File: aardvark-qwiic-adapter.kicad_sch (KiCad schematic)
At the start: 1 part, among them J1 Conn_02x05_Odd_Even

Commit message: Add LDO
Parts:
- added U1: AP7361C-33E, Package_TO_SOT_SMD:SOT-223-3_TabPin2, symbol Regulator_Linear:AP7361C-33E
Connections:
- net GND: now also U1.2 (GND)
- net at J1.4 (Pin_4): now also J1.6 (Pin_6), U1.1 (VI)
- new net +3.3V: U1.3 (VO)
- no-connect marks 2 -> 0
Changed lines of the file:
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@@
     (rev "1.0")
   )
-  (no_connect (at 148.59 93.98))
-  (no_connect (at 148.59 96.52))
+  (junction (at 151.13 93.98) (diameter 0) (color 0 0 0 0)
+  )
+  (wire (pts (xy 185.42 93.98) (xy 190.5 93.98))
+    (stroke (width 0) (type default))
+  )
   (wire (pts (xy 129.54 99.06) (xy 135.89 99.06))
+    (stroke (width 0) (type default))
+  )
+  (wire (pts (xy 190.5 93.98) (xy 190.5 92.71))
+    (stroke (width 0) (type default))
+  )
+  (wire (pts (xy 151.13 93.98) (xy 151.13 96.52))
     (stroke (width 0) (type default))
   )
@@
     (stroke (width 0) (type default))
   )
+  (wire (pts (xy 148.59 93.98) (xy 151.13 93.98))
+    (stroke (width 0) (type default))
+  )
+  (wire (pts (xy 151.13 93.98) (xy 170.18 93.98))
+    (stroke (width 0) (type default))
+  )
   (wire (pts (xy 148.59 91.44) (xy 156.21 91.44))
     (stroke (width 0) (type default))
@@
     (stroke (width 0) (type default))
   )
+  (wire (pts (xy 148.59 96.52) (xy 151.13 96.52))
+    (stroke (width 0) (type default))
+  )
   (wire (pts (xy 129.54 96.52) (xy 135.89 96.52))
+    (stroke (width 0) (type default))
+  )
+  (wire (pts (xy 177.8 101.6) (xy 177.8 102.87))
     (stroke (width 0) (type default))
   )
@@
     (effects (font (size 1.27 1.27)) (justify right bottom))
   )
+  (symbol (lib_id "power:GND") (at 177.8 102.87 0) (unit 1)
+    (in_bom yes) (on_board yes) (dnp no) (fields_autoplaced)
+    (property "Reference" "#PWR02" (at 177.8 109.22 0)
+      (effects (font (size 1.27 1.27)) hide)
+    )
+    (property "Value" "GND" (at 177.8 107.95 0)
+      (effects (font (size 1.27 1.27)))
+    )
+    (property "Footprint" "" (at 177.8 102.87 0)
+      (effects (font (size 1.27 1.27)) hide)
+    )
+    (property "Datasheet" "" (at 177.8 102.87 0)
+      (effects (font (size 1.27 1.27)) hide)
+    )
+    (pin "1")
+    (instances
+      (project "aardvark-qwiic-adapter"
+        (path "/dd35b9f1-2797-46a7-a3ff-4e2c1be5fc91"
+          (reference "#PWR02") (unit 1)
+        )
+      )
+    )
+  )
+  (symbol (lib_id "power:+3.3V") (at 190.5 92.71 0) (unit 1)
+    (in_bom yes) (on_board yes) (dnp no) (fields_autoplaced)
+    (property "Reference" "#PWR01" (at 190.5 96.52 0)
+      (effects (font (size 1.27 1.27)) hide)
+    )
+    (property "Value" "+3.3V" (at 190.5 88.9 0)
+      (effects (font (size 1.27 1.27)))
+    )
+    (property "Footprint" "" (at 190.5 92.71 0)
+      (effects (font (size 1.27 1.27)) hide)
+    )
+    (property "Datasheet" "" (at 190.5 92.71 0)
+      (effects (font (size 1.27 1.27)) hide)
+    )
+    (pin "1")
+    (instances
+      (project "aardvark-qwiic-adapter"
+        (path "/dd35b9f1-2797-46a7-a3ff-4e2c1be5fc91"
+          (reference "#PWR01") (unit 1)
+        )
+      )
+    )
+  )
+  (symbol (lib_id "Regulator_Linear:AP7361C-33E") (at 177.8 93.98 0) (unit 1)
+    (in_bom yes) (on_board yes) (dnp no) (fields_autoplaced)
+    (property "Reference" "U1" (at 177.8 87.63 0)
+      (effects (font (size 1.27 1.27)))
+    )
+    (property "Value" "AP7361C-33E" (at 177.8 90.17 0)
+      (effects (font (size 1.27 1.27)))
+    )
+    (property "Footprint" "Package_TO_SOT_SMD:SOT-223-3_TabPin2" (at 177.8 88.265 0)
+      (effects (font (size 1.27 1.27) italic) hide)
+    )
+    (property "Datasheet" "https://www.diodes.com/assets/Datasheets/AP7361C.pdf" (at 177.8 95.25 0)
+      (effects (font (size 1.27 1.27)) hide)
+    )
+    (pin "1")
+    (pin "2")
+    (pin "3")
+    (instances
+      (project "aardvark-qwiic-adapter"
+        (path "/dd35b9f1-2797-46a7-a3ff-4e2c1be5fc91"
+          (reference "U1") (unit 1)
+        )
+      )
+    )
+  )
   (symbol (lib_id "Connector_Generic:Conn_02x05_Odd_Even") (at 140.97 96.52 0) (unit 1)

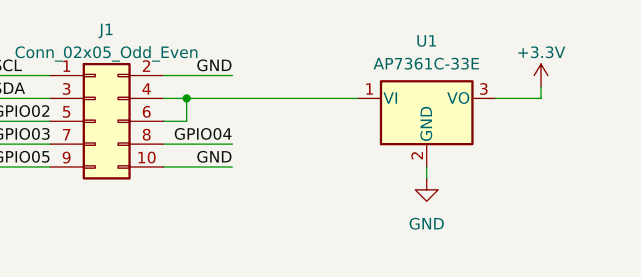
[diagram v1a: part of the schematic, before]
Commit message: Caps on LDO
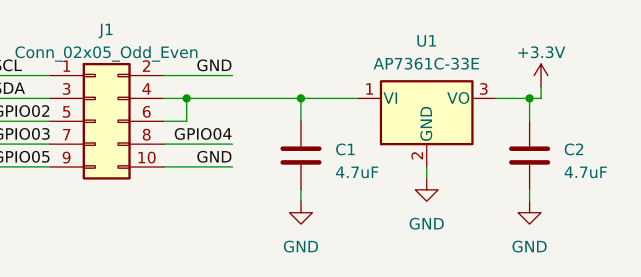
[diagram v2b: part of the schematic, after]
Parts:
- added C1, C2: 4.7uF, Capacitor_SMD:C_0805_2012Metric, symbol Device:C
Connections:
- net +3.3V: now also C2.1
- net GND: now also C1.2, C2.2
- net at J1.4 (Pin_4), J1.6 (Pin_6), U1.1 (VI): now also C1.1
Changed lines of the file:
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@@
   (junction (at 151.13 93.98) (diameter 0) (color 0 0 0 0)
   )
-  (wire (pts (xy 185.42 93.98) (xy 190.5 93.98))
+  (junction (at 189.23 93.98) (diameter 0) (color 0 0 0 0)
+  )
+  (junction (at 163.83 93.98) (diameter 0) (color 0 0 0 0)
+  )
+  (wire (pts (xy 163.83 93.98) (xy 170.18 93.98))
+    (stroke (width 0) (type default))
+  )
+  (wire (pts (xy 163.83 93.98) (xy 163.83 96.52))
+    (stroke (width 0) (type default))
+  )
+  (wire (pts (xy 185.42 93.98) (xy 189.23 93.98))
     (stroke (width 0) (type default))
   )
@@
     (stroke (width 0) (type default))
   )
+  (wire (pts (xy 189.23 93.98) (xy 189.23 96.52))
+    (stroke (width 0) (type default))
+  )
   (wire (pts (xy 129.54 101.6) (xy 135.89 101.6))
     (stroke (width 0) (type default))
@@
     (stroke (width 0) (type default))
   )
-  (wire (pts (xy 151.13 93.98) (xy 170.18 93.98))
+  (wire (pts (xy 151.13 93.98) (xy 163.83 93.98))
     (stroke (width 0) (type default))
   )
@@
     (stroke (width 0) (type default))
   )
+  (wire (pts (xy 163.83 104.14) (xy 163.83 105.41))
+    (stroke (width 0) (type default))
+  )
   (wire (pts (xy 148.59 96.52) (xy 151.13 96.52))
     (stroke (width 0) (type default))
@@
   )
   (wire (pts (xy 177.8 101.6) (xy 177.8 102.87))
+    (stroke (width 0) (type default))
+  )
+  (wire (pts (xy 189.23 93.98) (xy 190.5 93.98))
+    (stroke (width 0) (type default))
+  )
+  (wire (pts (xy 189.23 104.14) (xy 189.23 105.41))
     (stroke (width 0) (type default))
   )
@@
     (effects (font (size 1.27 1.27)) (justify right bottom))
   )
+  (symbol (lib_id "Device:C") (at 163.83 100.33 0) (unit 1)
+    (in_bom yes) (on_board yes) (dnp no) (fields_autoplaced)
+    (property "Reference" "C1" (at 167.64 99.695 0)
+      (effects (font (size 1.27 1.27)) (justify left))
+    )
+    (property "Value" "4.7uF" (at 167.64 102.235 0)
+      (effects (font (size 1.27 1.27)) (justify left))
+    )
+    (property "Footprint" "Capacitor_SMD:C_0805_2012Metric" (at 164.7952 104.14 0)
+      (effects (font (size 1.27 1.27)) hide)
+    )
+    (property "Datasheet" "~" (at 163.83 100.33 0)
+      (effects (font (size 1.27 1.27)) hide)
+    )
+    (pin "1")
+    (pin "2")
+    (instances
+      (project "aardvark-qwiic-adapter"
+        (path "/dd35b9f1-2797-46a7-a3ff-4e2c1be5fc91"
+          (reference "C1") (unit 1)
+        )
+      )
+    )
+  )
+  (symbol (lib_id "power:GND") (at 163.83 105.41 0) (unit 1)
+    (in_bom yes) (on_board yes) (dnp no) (fields_autoplaced)
+    (property "Reference" "#PWR03" (at 163.83 111.76 0)
+      (effects (font (size 1.27 1.27)) hide)
+    )
+    (property "Value" "GND" (at 163.83 110.49 0)
+      (effects (font (size 1.27 1.27)))
+    )
+    (property "Footprint" "" (at 163.83 105.41 0)
+      (effects (font (size 1.27 1.27)) hide)
+    )
+    (property "Datasheet" "" (at 163.83 105.41 0)
+      (effects (font (size 1.27 1.27)) hide)
+    )
+    (pin "1")
+    (instances
+      (project "aardvark-qwiic-adapter"
+        (path "/dd35b9f1-2797-46a7-a3ff-4e2c1be5fc91"
+          (reference "#PWR03") (unit 1)
+        )
+      )
+    )
+  )
+  (symbol (lib_id "power:GND") (at 189.23 105.41 0) (unit 1)
+    (in_bom yes) (on_board yes) (dnp no) (fields_autoplaced)
+    (property "Reference" "#PWR04" (at 189.23 111.76 0)
+      (effects (font (size 1.27 1.27)) hide)
+    )
+    (property "Value" "GND" (at 189.23 110.49 0)
+      (effects (font (size 1.27 1.27)))
+    )
+    (property "Footprint" "" (at 189.23 105.41 0)
+      (effects (font (size 1.27 1.27)) hide)
+    )
+    (property "Datasheet" "" (at 189.23 105.41 0)
+      (effects (font (size 1.27 1.27)) hide)
+    )
+    (pin "1")
+    (instances
+      (project "aardvark-qwiic-adapter"
+        (path "/dd35b9f1-2797-46a7-a3ff-4e2c1be5fc91"
+          (reference "#PWR04") (unit 1)
+        )
+      )
+    )
+  )
   (symbol (lib_id "power:GND") (at 177.8 102.87 0) (unit 1)
     (in_bom yes) (on_board yes) (dnp no) (fields_autoplaced)
@@
         )
       )
+    )
+  )
+  (symbol (lib_id "Device:C") (at 189.23 100.33 0) (unit 1)
+    (in_bom yes) (on_board yes) (dnp no) (fields_autoplaced)
+    (property "Reference" "C2" (at 193.04 99.695 0)
+      (effects (font (size 1.27 1.27)) (justify left))
+    )
+    (property "Value" "4.7uF" (at 193.04 102.235 0)
+      (effects (font (size 1.27 1.27)) (justify left))
+    )
+    (property "Footprint" "Capacitor_SMD:C_0805_2012Metric" (at 190.1952 104.14 0)
+      (effects (font (size 1.27 1.27)) hide)
+    )
+    (property "Datasheet" "~" (at 189.23 100.33 0)
+      (effects (font (size 1.27 1.27)) hide)
+    )
+    (pin "1")
+    (pin "2")
+    (instances
+      (project "aardvark-qwiic-adapter"
+        (path "/dd35b9f1-2797-46a7-a3ff-4e2c1be5fc91"
+          (reference "C2") (unit 1)
+        )
+      )

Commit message: QWIIC connector
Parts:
- added J2: Conn_01x04, Connector_JST:JST_SH_BM04B-SRSS-TB_1x04-1MP_P1.00mm_Vertical, symbol Connector_Generic:Conn_01x04
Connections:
- net +3.3V: now also J2.3 (Pin_3)
- net GND: now also J2.4 (Pin_4)
- net SCL: now also J2.1 (Pin_1)
- net SDA: now also J2.2 (Pin_2)
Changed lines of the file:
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@@
+    (stroke (width 0) (type default))
+  )
+  (wire (pts (xy 83.82 96.52) (xy 91.44 96.52))
     (stroke (width 0) (type default))
   )
@@
     (stroke (width 0) (type default))
   )
+  (wire (pts (xy 83.82 99.06) (xy 91.44 99.06))
+    (stroke (width 0) (type default))
+  )
   (wire (pts (xy 189.23 93.98) (xy 189.23 96.52))
     (stroke (width 0) (type default))
@@
     (stroke (width 0) (type default))
   )
+  (wire (pts (xy 83.82 93.98) (xy 91.44 93.98))
+    (stroke (width 0) (type default))
+  )
   (wire (pts (xy 148.59 91.44) (xy 156.21 91.44))
     (stroke (width 0) (type default))
@@
   )
   (wire (pts (xy 148.59 96.52) (xy 151.13 96.52))
+    (stroke (width 0) (type default))
+  )
+  (wire (pts (xy 83.82 91.44) (xy 91.44 91.44))
     (stroke (width 0) (type default))
   )
@@
     (effects (font (size 1.27 1.27)) (justify right bottom))
   )
+  (label "GND" (at 83.82 99.06 0) (fields_autoplaced)
+    (effects (font (size 1.27 1.27)) (justify left bottom))
+  )
+  (label "SDA" (at 83.82 93.98 0) (fields_autoplaced)
+    (effects (font (size 1.27 1.27)) (justify left bottom))
+  )
+  (label "SCL" (at 83.82 91.44 0) (fields_autoplaced)
+    (effects (font (size 1.27 1.27)) (justify left bottom))
+  )
+  (label "+3.3V" (at 83.82 96.52 0) (fields_autoplaced)
+    (effects (font (size 1.27 1.27)) (justify left bottom))
+  )
   (symbol (lib_id "Device:C") (at 163.83 100.33 0) (unit 1)
     (in_bom yes) (on_board yes) (dnp no) (fields_autoplaced)
@@
         )
       )
+    )
+  )
+  (symbol (lib_id "Connector_Generic:Conn_01x04") (at 96.52 93.98 0) (unit 1)
+    (in_bom yes) (on_board yes) (dnp no) (fields_autoplaced)
+    (property "Reference" "J2" (at 99.06 94.615 0)
+      (effects (font (size 1.27 1.27)) (justify left))
+    )
+    (property "Value" "Conn_01x04" (at 99.06 97.155 0)
+      (effects (font (size 1.27 1.27)) (justify left))
+    )
+    (property "Footprint" "Connector_JST:JST_SH_BM04B-SRSS-TB_1x04-1MP_P1.00mm_Vertical" (at 96.52 93.98 0)
+      (effects (font (size 1.27 1.27)) hide)
+    )
+    (property "Datasheet" "~" (at 96.52 93.98 0)
+      (effects (font (size 1.27 1.27)) hide)
+    )
+    (pin "1")
+    (pin "2")
+    (pin "3")
+    (pin "4")
+    (instances
+      (project "aardvark-qwiic-adapter"
+        (path "/dd35b9f1-2797-46a7-a3ff-4e2c1be5fc91"
+          (reference "J2") (unit 1)
+        )
+      )

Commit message: Title block
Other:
- title: Aardvark I2C Breakout -> Aardvark QWIIC Adapter
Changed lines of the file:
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@@
   (paper "USLetter")
   (title_block
-    (title "Aardvark I2C Breakout")
-    (date "2023-02-18")
+    (title "Aardvark QWIIC Adapter")
+    (date "2023-02-19")
     (rev "1.0")
   )

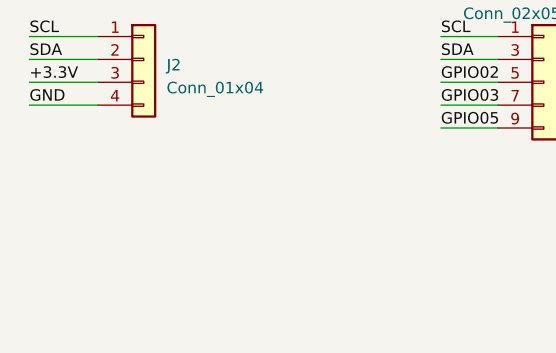
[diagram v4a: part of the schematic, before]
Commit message: GPIO breakout
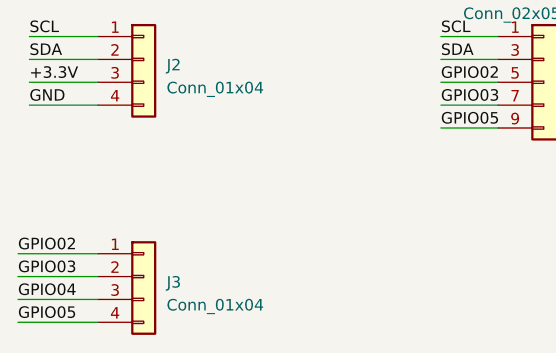
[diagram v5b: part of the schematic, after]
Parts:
- added J3: Conn_01x04, Connector_PinHeader_2.54mm:PinHeader_1x04_P2.54mm_Vertical, symbol Connector_Generic:Conn_01x04
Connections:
- net GPIO02: now also J3.1 (Pin_1)
- net GPIO03: now also J3.2 (Pin_2)
- net GPIO04: now also J3.3 (Pin_3)
- net GPIO05: now also J3.4 (Pin_4)
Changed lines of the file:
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@@
+    (stroke (width 0) (type default))
+  )
+  (wire (pts (xy 82.55 115.57) (xy 91.44 115.57))
     (stroke (width 0) (type default))
   )
@@
     (stroke (width 0) (type default))
   )
+  (wire (pts (xy 82.55 120.65) (xy 91.44 120.65))
+    (stroke (width 0) (type default))
+  )
   (wire (pts (xy 148.59 93.98) (xy 151.13 93.98))
     (stroke (width 0) (type default))
@@
     (stroke (width 0) (type default))
   )
+  (wire (pts (xy 82.55 118.11) (xy 91.44 118.11))
+    (stroke (width 0) (type default))
+  )
   (wire (pts (xy 148.59 99.06) (xy 156.21 99.06))
     (stroke (width 0) (type default))
@@
     (stroke (width 0) (type default))
   )
+  (wire (pts (xy 82.55 123.19) (xy 91.44 123.19))
+    (stroke (width 0) (type default))
+  )
   (wire (pts (xy 189.23 104.14) (xy 189.23 105.41))
     (stroke (width 0) (type default))
@@
   )
   (label "SCL" (at 129.54 91.44 0) (fields_autoplaced)
+    (effects (font (size 1.27 1.27)) (justify left bottom))
+  )
+  (label "GPIO04" (at 82.55 120.65 0) (fields_autoplaced)
     (effects (font (size 1.27 1.27)) (justify left bottom))
   )
@@
     (effects (font (size 1.27 1.27)) (justify right bottom))
   )
+  (label "GPIO05" (at 82.55 123.19 0) (fields_autoplaced)
+    (effects (font (size 1.27 1.27)) (justify left bottom))
+  )
   (label "GND" (at 156.21 101.6 180) (fields_autoplaced)
     (effects (font (size 1.27 1.27)) (justify right bottom))
@@
     (effects (font (size 1.27 1.27)) (justify left bottom))
   )
+  (label "GPIO03" (at 82.55 118.11 0) (fields_autoplaced)
+    (effects (font (size 1.27 1.27)) (justify left bottom))
+  )
+  (label "GPIO02" (at 82.55 115.57 0) (fields_autoplaced)
+    (effects (font (size 1.27 1.27)) (justify left bottom))
+  )
   (label "SDA" (at 129.54 93.98 0) (fields_autoplaced)
     (effects (font (size 1.27 1.27)) (justify left bottom))
@@
         )
       )
+    )
+  )
+  (symbol (lib_id "Connector_Generic:Conn_01x04") (at 96.52 118.11 0) (unit 1)
+    (in_bom yes) (on_board yes) (dnp no) (fields_autoplaced)
+    (property "Reference" "J3" (at 99.06 118.745 0)
+      (effects (font (size 1.27 1.27)) (justify left))
+    )
+    (property "Value" "Conn_01x04" (at 99.06 121.285 0)
+      (effects (font (size 1.27 1.27)) (justify left))
+    )
+    (property "Footprint" "Connector_PinHeader_2.54mm:PinHeader_1x04_P2.54mm_Vertical" (at 96.52 118.11 0)
+      (effects (font (size 1.27 1.27)) hide)
+    )
+    (property "Datasheet" "~" (at 96.52 118.11 0)
+      (effects (font (size 1.27 1.27)) hide)
+    )
+    (pin "1")
+    (pin "2")
+    (pin "3")
+    (pin "4")
+    (instances
+      (project "aardvark-qwiic-adapter"
+        (path "/dd35b9f1-2797-46a7-a3ff-4e2c1be5fc91"
+          (reference "J3") (unit 1)
+        )
+      )

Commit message: Power jumper
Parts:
- added J4: Conn_01x02, Connector_PinHeader_2.54mm:PinHeader_1x02_P2.54mm_Vertical, symbol Connector_Generic:Conn_01x02
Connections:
- net +3.3V: now also J4.1 (Pin_1); no longer J2.3 (Pin_3)
- new net: J2.3 (Pin_3), J4.2 (Pin_2)
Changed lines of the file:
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@@
+    (stroke (width 0) (type default))
+  )
+  (wire (pts (xy 74.93 93.98) (xy 71.12 93.98))
     (stroke (width 0) (type default))
   )
@@
     (stroke (width 0) (type default))
   )
-  (wire (pts (xy 83.82 96.52) (xy 91.44 96.52))
-    (stroke (width 0) (type default))
-  )
   (wire (pts (xy 151.13 93.98) (xy 151.13 96.52))
     (stroke (width 0) (type default))
@@
     (stroke (width 0) (type default))
   )
+  (wire (pts (xy 71.12 96.52) (xy 91.44 96.52))
+    (stroke (width 0) (type default))
+  )
   (wire (pts (xy 163.83 104.14) (xy 163.83 105.41))
     (stroke (width 0) (type default))
@@
   )
   (wire (pts (xy 189.23 104.14) (xy 189.23 105.41))
+    (stroke (width 0) (type default))
+  )
+  (wire (pts (xy 74.93 91.44) (xy 74.93 93.98))
     (stroke (width 0) (type default))
   )
@@
   )
   (label "SCL" (at 83.82 91.44 0) (fields_autoplaced)
-    (effects (font (size 1.27 1.27)) (justify left bottom))
-  )
-  (label "+3.3V" (at 83.82 96.52 0) (fields_autoplaced)
     (effects (font (size 1.27 1.27)) (justify left bottom))
   )
@@
     )
   )
+  (symbol (lib_id "Connector_Generic:Conn_01x02") (at 66.04 93.98 0) (mirror y) (unit 1)
+    (in_bom yes) (on_board yes) (dnp no)
+    (property "Reference" "J4" (at 63.5 94.615 0)
+      (effects (font (size 1.27 1.27)) (justify left))
+    )
+    (property "Value" "Conn_01x02" (at 63.5 97.155 0)
+      (effects (font (size 1.27 1.27)) (justify left))
+    )
+    (property "Footprint" "Connector_PinHeader_2.54mm:PinHeader_1x02_P2.54mm_Vertical" (at 66.04 93.98 0)
+      (effects (font (size 1.27 1.27)) hide)
+    )
+    (property "Datasheet" "~" (at 66.04 93.98 0)
+      (effects (font (size 1.27 1.27)) hide)
+    )
+    (pin "1")
+    (pin "2")
+    (instances
+      (project "aardvark-qwiic-adapter"
+        (path "/dd35b9f1-2797-46a7-a3ff-4e2c1be5fc91"
+          (reference "J4") (unit 1)
+        )
+      )
+    )
+  )
   (symbol (lib_id "power:GND") (at 163.83 105.41 0) (unit 1)
     (in_bom yes) (on_board yes) (dnp no) (fields_autoplaced)
@@
         )
       )
+    )
+  )
+  (symbol (lib_id "power:+3.3V") (at 74.93 91.44 0) (unit 1)
+    (in_bom yes) (on_board yes) (dnp no) (fields_autoplaced)
+    (property "Reference" "#PWR05" (at 74.93 95.25 0)
+      (effects (font (size 1.27 1.27)) hide)
+    )
+    (property "Value" "+3.3V" (at 74.93 87.63 0)
+      (effects (font (size 1.27 1.27)))
+    )
+    (property "Footprint" "" (at 74.93 91.44 0)
+      (effects (font (size 1.27 1.27)) hide)
+    )
+    (property "Datasheet" "" (at 74.93 91.44 0)
+      (effects (font (size 1.27 1.27)) hide)
+    )
+    (pin "1")
+    (instances
+      (project "aardvark-qwiic-adapter"
+        (path "/dd35b9f1-2797-46a7-a3ff-4e2c1be5fc91"
+          (reference "#PWR05") (unit 1)
+        )
+      )
